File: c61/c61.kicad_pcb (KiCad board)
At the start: 2 copper layers, 23 x 37 mm, 16 parts, among them J1 Conn_01x14, U1 ESP32-C61HF4, U2 TPS63900DSKR, Y1 Crystal

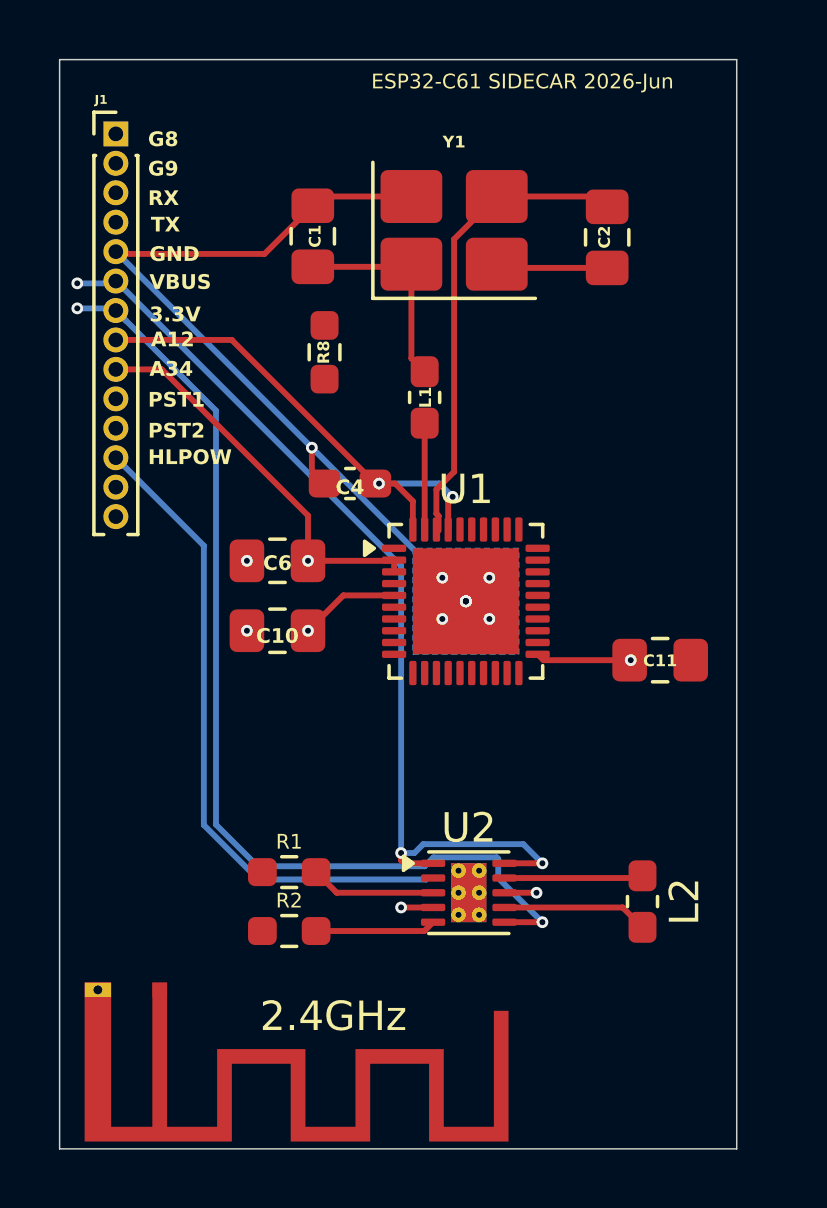
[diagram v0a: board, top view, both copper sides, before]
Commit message: c61 bare done
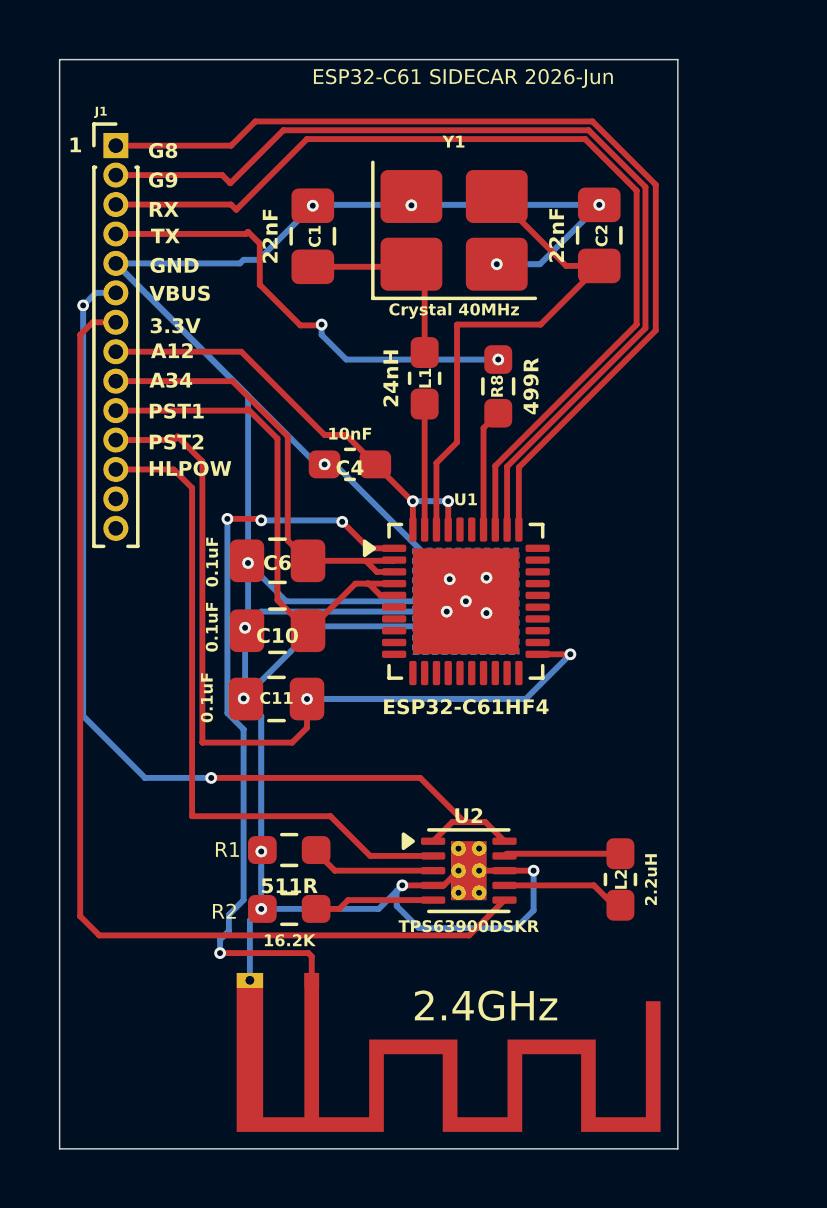
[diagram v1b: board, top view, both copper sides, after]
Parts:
- J1: value Conn_01x14 -> 1x14
- R1: value 511 -> 511R
- R8: value 499 -> 499R
- Y1: value Crystal -> Crystal 40MHz
- moved C11 13.1 mm to (136.4, 111.7), turned to 180 degrees
- moved R8 6.01 mm to (143.9, 101.1)
- moved 2.4GHz 5.17 mm to (137.6, 121.3)
- moved L2 1.06 mm to (148.1, 117.8)
- moved R1 0.75 mm to (136.8, 116.8)
- moved R2 0.75 mm to (136.8, 118.8)
- moved U2 0.75 mm to (142.9, 117.5)
- moved C4 0.65 mm to (138.9, 103.8)
- moved L1 0.65 mm to (141.4, 100.8)
- moved J1 0.40 mm to (130.9, 92.9)
- moved C2 0.28 mm to (147.3, 96.0), turned to -90 degrees
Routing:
- net GND: track 33.8 -> 104.9 mm, vias 13 -> 17
- net Net-(J1-Pin_2): track 0.00 -> 33.2 mm
- net Net-(J1-Pin_1): track 0.00 -> 33.2 mm
- net Net-(J1-Pin_3): track 0.00 -> 33.0 mm
- net /ANT: track 0.00 -> 25.4 mm, vias 0 -> 4
- net /PST2: track 3.21 -> 28.3 mm, vias 1 -> 2
- net Net-(J1-Pin_4): track 0.00 -> 16.0 mm, vias 0 -> 2
- net /PST1: track 3.42 -> 17.6 mm, vias 1 -> 0
- net Net-(U1-U0TXD): track 0.00 -> 4.16 mm
- net /A12: track 17.2 -> 15.3 mm
- net /3.3V: track 34.6 -> 36.3 mm, vias 2 -> 0
- net /A34: track 13.5 -> 15.2 mm, vias 1 -> 0
- net Net-(U1-XTAL_N): track 16.1 -> 17.4 mm
- net Net-(U2-LX2): track 4.97 -> 4.22 mm
- net Net-(U2-LX1): track 4.72 -> 3.97 mm
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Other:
- board size 23 x 37 mm -> 21 x 37 mm
- board text added: "1"

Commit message: no epaper this time
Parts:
- added J2: SFV24R-EPAPER, somethingfootprints:SFV24R3STBE1HLF, F.Cu at (9.90, 4.00)
